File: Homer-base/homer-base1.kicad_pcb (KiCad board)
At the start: 2 copper layers, 16 parts

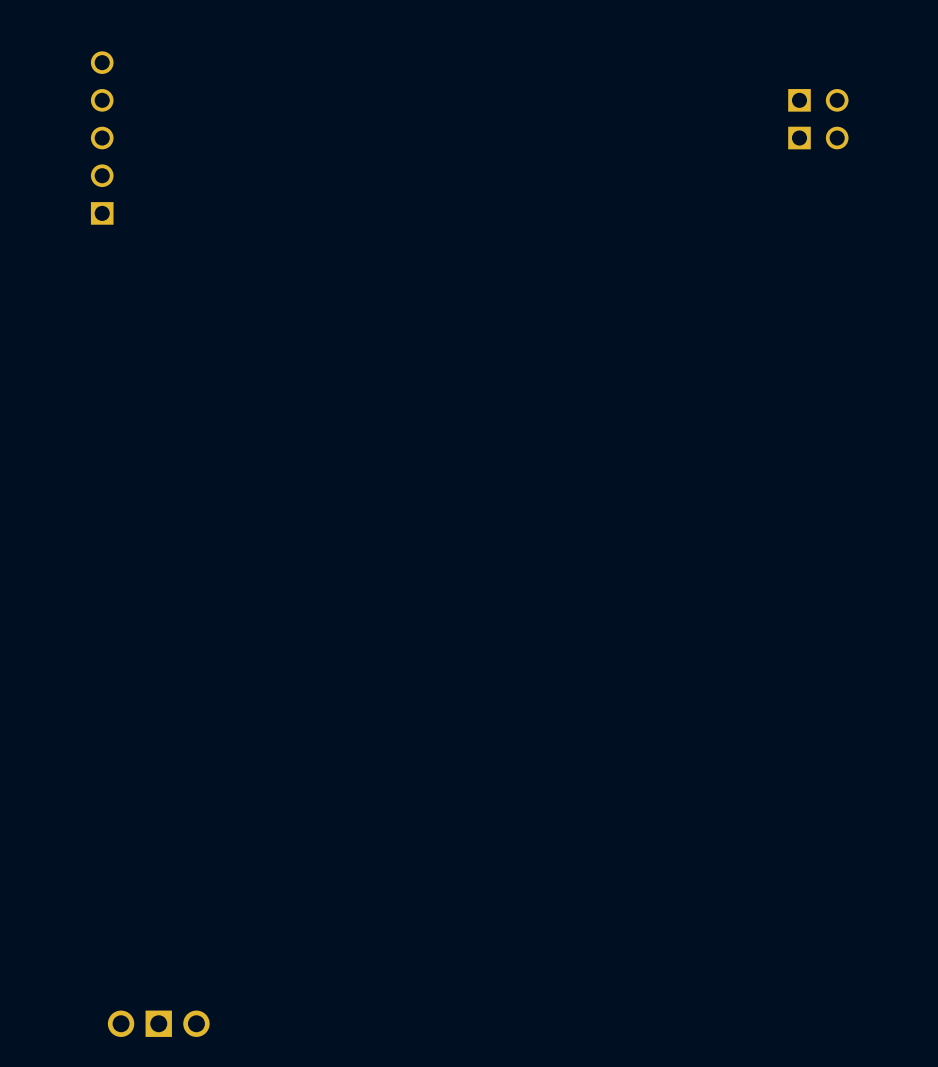
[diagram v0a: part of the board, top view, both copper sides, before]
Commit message: Add varistor and AC/DC
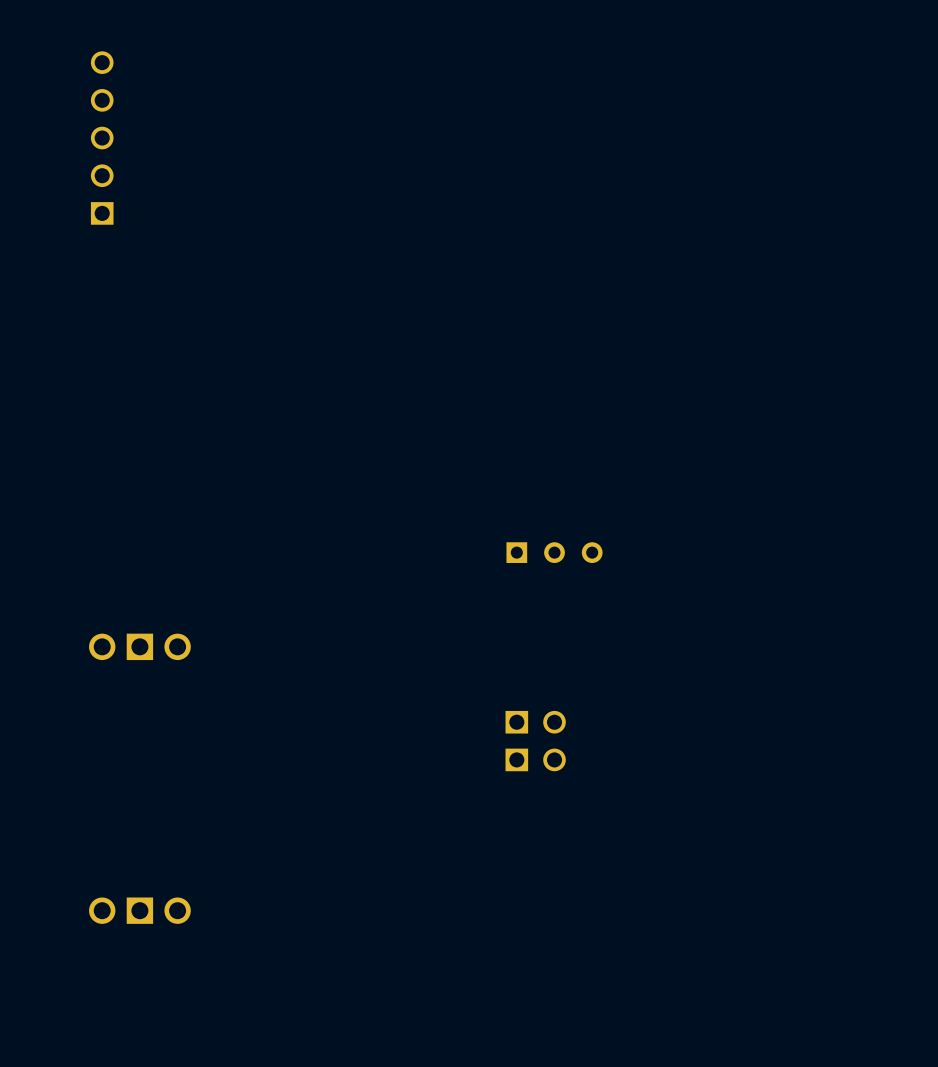
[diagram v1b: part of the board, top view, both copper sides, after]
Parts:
- added LD1086D: , LM78XXV, F.Cu at (1.27, -789.9)
- added Selettore Power: Val**, SIL-3, F.Cu at (29.2, -796.3)
- moved ? 46.0 mm to (27.9, -784.9)
- moved RS232 46.0 mm to (27.9, -782.3)
- moved LM7805V 7.73 mm to (1.27, -772.2)
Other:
- board text added: "220V"
- board text added: "3,6V,NC,NC,NC,B4,B2,SCA,RST"
- board text added: "6V"
- board text added: "GND,NC,NC,B5,B3,B1,SCL,BL"
- board text removed: "3,6V"
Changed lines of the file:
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@@
     (area -31.03245 -878.940001 169.316401 -756.819999)
     (thickness 1.6)
-    (drawings 27)
+    (drawings 29)
     (tracks 0)
     (zones 0)
-    (modules 16)
+    (modules 18)
     (nets 23)
   )
@@
     (add_net VCC)
   )
+  (module LM78XXV (layer "Rame Fronte")
+    (at 1.27 -789.94 270)
+    (descr "Regulateur TO220 serie LM78xx")
+    (tags "TR TO220")
+    (fp_text reference LD1086D (at 3.81 0 360) (layer "Serigrafia Fronte")
+      (effects (font (size 1.524 1.016) (thickness 0.2032)))
+    )
+    (fp_text value "" (at -3.175 -0.635 360) (layer "Serigrafia Fronte")
+      (effects (font (size 1.524 1.016) (thickness 0.2032)))
+    )
+    (fp_line (start 1.905 -4.445) (end 2.54 -4.445) (layer "Serigrafia Fronte") (width 0.254))
+    (fp_line (start 2.54 -4.445) (end 2.54 4.445) (layer "Serigrafia Fronte") (width 0.254))
+    (fp_line (start 2.54 4.445) (end 1.905 4.445) (layer "Serigrafia Fronte") (width 0.254))
+    (fp_line (start -1.905 -4.445) (end 1.905 -4.445) (layer "Serigrafia Fronte") (width 0.254))
+    (fp_line (start 1.905 -4.445) (end 1.905 4.445) (layer "Serigrafia Fronte") (width 0.254))
+    (fp_line (start 1.905 4.445) (end -1.905 4.445) (layer "Serigrafia Fronte") (width 0.254))
+    (fp_line (start -1.905 4.445) (end -1.905 -4.445) (layer "Serigrafia Fronte") (width 0.254))
+    (pad VI thru_hole circle (at 0 -2.54 270) (size 1.778 1.778) (drill 1.143)
+      (layers *.Cu *.Mask "Serigrafia Fronte")
+    )
+    (pad GND thru_hole rect (at 0 0 270) (size 1.778 1.778) (drill 1.143)
+      (layers *.Cu *.Mask "Serigrafia Fronte")
+    )
+    (pad VO thru_hole circle (at 0 2.54 270) (size 1.778 1.778) (drill 1.143)
+      (layers *.Cu *.Mask "Serigrafia Fronte")
+    )
+  )
   (module VASCH8x2 (layer "Rame Fronte")
     (at 6.35 -852.17 180)
@@
   )
   (module PIN_ARRAY_2X1 (layer "Rame Fronte")
-    (at 46.99 -826.77)
+    (at 27.94 -784.86)
     (descr "Connecteurs 2 pins")
     (tags "CONN DEV")
@@
   )
   (module PIN_ARRAY_2X1   placed (layer "Rame Fronte")
-    (at 46.99 -824.23)
+    (at 27.94 -782.32)
     (descr "Connecteurs 2 pins")
     (tags "CONN DEV")
@@
   )
   (module LM78XXV (layer "Rame Fronte")
-    (at 2.54 -764.54 270)
+    (at 1.27 -772.16 270)
     (descr "Regulateur TO220 serie LM78xx")
     (tags "TR TO220")
@@
     )
   )
+  (module SIL-3 (layer "Rame Fronte")
+    (at 29.21 -796.29)
+    (descr "Connecteur 3 pins")
+    (tags "CONN DEV")
+    (fp_text reference "Selettore Power" (at 0 -3.81) (layer "Serigrafia Fronte")
+      (effects (font (size 1.7907 1.07696) (thickness 0.26924)))
+    )
+    (fp_text value Val** (at 0 -2.54) (layer "Serigrafia Fronte") hide
+      (effects (font (size 1.524 1.016) (thickness 0.3048)))
+    )
+    (fp_line (start -3.81 1.27) (end -3.81 -1.27) (layer "Serigrafia Fronte") (width 0.3048))
+    (fp_line (start -3.81 -1.27) (end 3.81 -1.27) (layer "Serigrafia Fronte") (width 0.3048))
+    (fp_line (start 3.81 -1.27) (end 3.81 1.27) (layer "Serigrafia Fronte") (width 0.3048))
+    (fp_line (start 3.81 1.27) (end -3.81 1.27) (layer "Serigrafia Fronte") (width 0.3048))
+    (fp_line (start -1.27 -1.27) (end -1.27 1.27) (layer "Serigrafia Fronte") (width 0.3048))
+    (pad 1 thru_hole rect (at -2.54 0) (size 1.397 1.397) (drill 0.8128)
+      (layers *.Cu *.Mask "Serigrafia Fronte")
+    )
+    (pad 2 thru_hole circle (at 0 0) (size 1.397 1.397) (drill 0.8128)
+      (layers *.Cu *.Mask "Serigrafia Fronte")
+    )
+    (pad 3 thru_hole circle (at 2.54 0) (size 1.397 1.397) (drill 0.8128)
+      (layers *.Cu *.Mask "Serigrafia Fronte")
+    )
+  )
+  (gr_text 6V (at 21.59 -796.29) (layer "Serigrafia Fronte")
+    (effects (font (size 1.5 1.5) (thickness 0.3)))
+  )
+  (gr_text 220V (at 36.83 -796.29) (layer "Serigrafia Fronte")
+    (effects (font (size 1.5 1.5) (thickness 0.3)))
+  )
   (gr_text LV (at 83.82 -814.07) (layer "Serigrafia Fronte")
     (effects (font (size 1.5 1.5) (thickness 0.3)))
@@
     (effects (font (size 1.5 1.5) (thickness 0.3)))
   )
-  (gr_text "3,3V BLU/NERO" (at 10.16 -829.31) (layer "Serigrafia Fronte")
-    (effects (font (size 1.5 1.5) (thickness 0.3)))
-  )
-  (gr_text GND (at 3.81 -819.15) (layer "Serigrafia Fronte")
-    (effects (font (size 1.5 1.5) (thickness 0.3)))
-  )
-  (gr_text "3,6V GIALLO/BLU" (at 10.16 -826.77) (layer "Serigrafia Fronte")
-    (effects (font (size 1.5 1.5) (thickness 0.3)))
-  )
-  (gr_text 1 (at 16.51 -858.52) (layer "Serigrafia Fronte")
+  (gr_text "3,3V BLU/NERO" (at 10.16 -819.15) (layer "Serigrafia Fronte")
+    (effects (font (size 1.5 1.5) (thickness 0.3)))
+  )
+  (gr_text GND (at 3.81 -829.31) (layer "Serigrafia Fronte")
+    (effects (font (size 1.5 1.5) (thickness 0.3)))
+  )
+  (gr_text "3,6V GIALLO/BLU" (at 11.43 -821.69) (layer "Serigrafia Fronte")
+    (effects (font (size 1.5 1.5) (thickness 0.3)))
+  )
+  (gr_text 1 (at 21.59 -854.71) (layer "Serigrafia Fronte")
     (effects (font (size 1.5 1.5) (thickness 0.3)))
   )
@@
     (effects (font (size 1.5 1.5) (thickness 0.3)))
   )
-  (gr_text 3,6V (at -3.81 -845.82) (layer "Serigrafia Fronte")
-    (effects (font (size 1.5 1.5) (thickness 0.3)))
-  )
-  (gr_text GND (at -3.81 -858.52) (layer "Serigrafia Fronte")
-    (effects (font (size 1.5 1.5) (thickness 0.3)))
-  )
-  (gr_text "ACQUA-A5 TX" (at 58.42 -824.23) (layer "Serigrafia Fronte")
-    (effects (font (size 1.5 1.5) (thickness 0.3)))
-  )
-  (gr_text "ACQUA-A5 RX" (at 58.42 -826.77) (layer "Serigrafia Fronte")
-    (effects (font (size 1.5 1.5) (thickness 0.3)))
-  )
+  (gr_text 3,6V,NC,NC,NC,B4,B2,SCA,RST (at 6.35 -845.82) (layer "Serigrafia Fronte")
+    (effects (font (size 1.5 1.5) (thickness 0.3)))
+  )
+  (gr_text GND,NC,NC,B5,B3,B1,SCL,BL (at 6.35 -858.52) (layer "Serigrafia Fronte")
+    (effects (font (size 1.5 1.5) (thickness 0.3)))
+  )
+  (gr_text "ACQUA-A5 TX" (at 39.37 -782.32) (layer "Serigrafia Fronte")
+    (effects (font (size 1.5 1.5) (thickness 0.3)))
+  )
+  (gr_text "ACQUA-A5 RX" (at 39.37 -784.86) (layer "Serigrafia Fronte")
+    (effects (font (size 1.5 1.5) (thickness 0.3)))
+  )

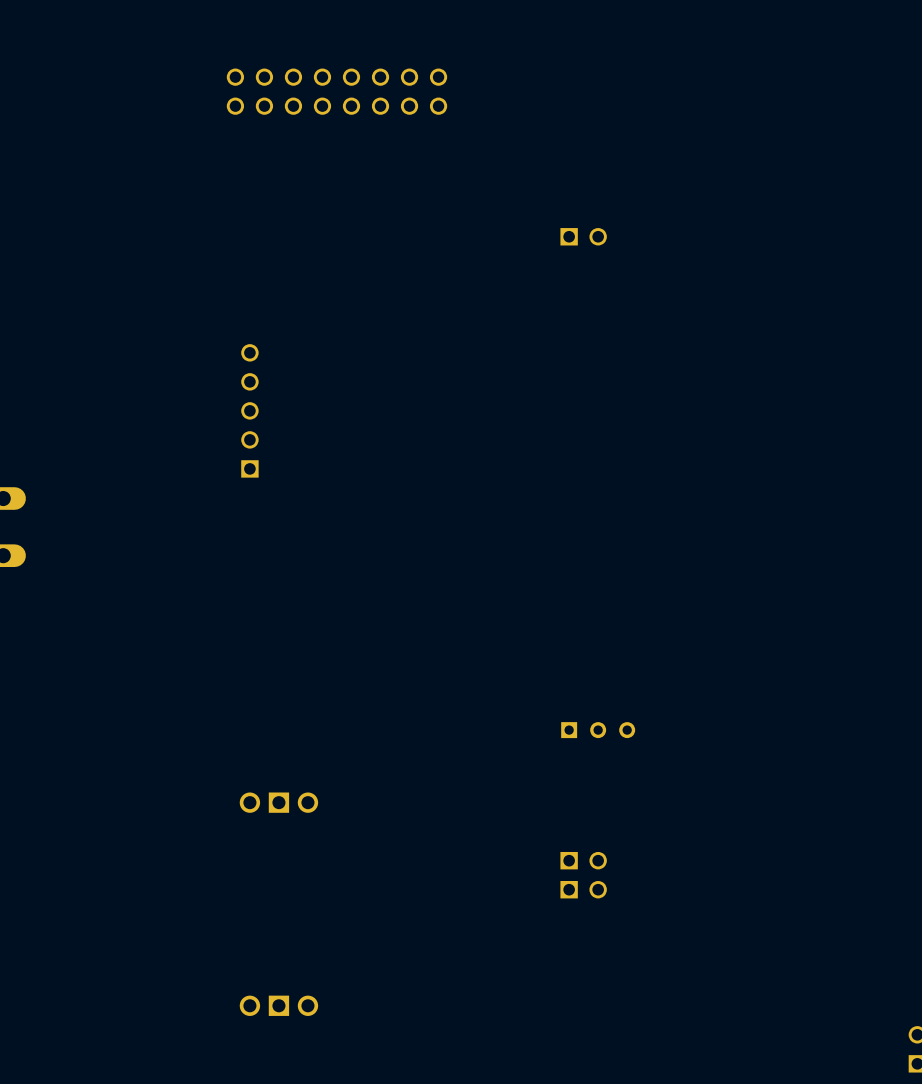
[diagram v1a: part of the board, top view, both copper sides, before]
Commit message: New power supply subsystem
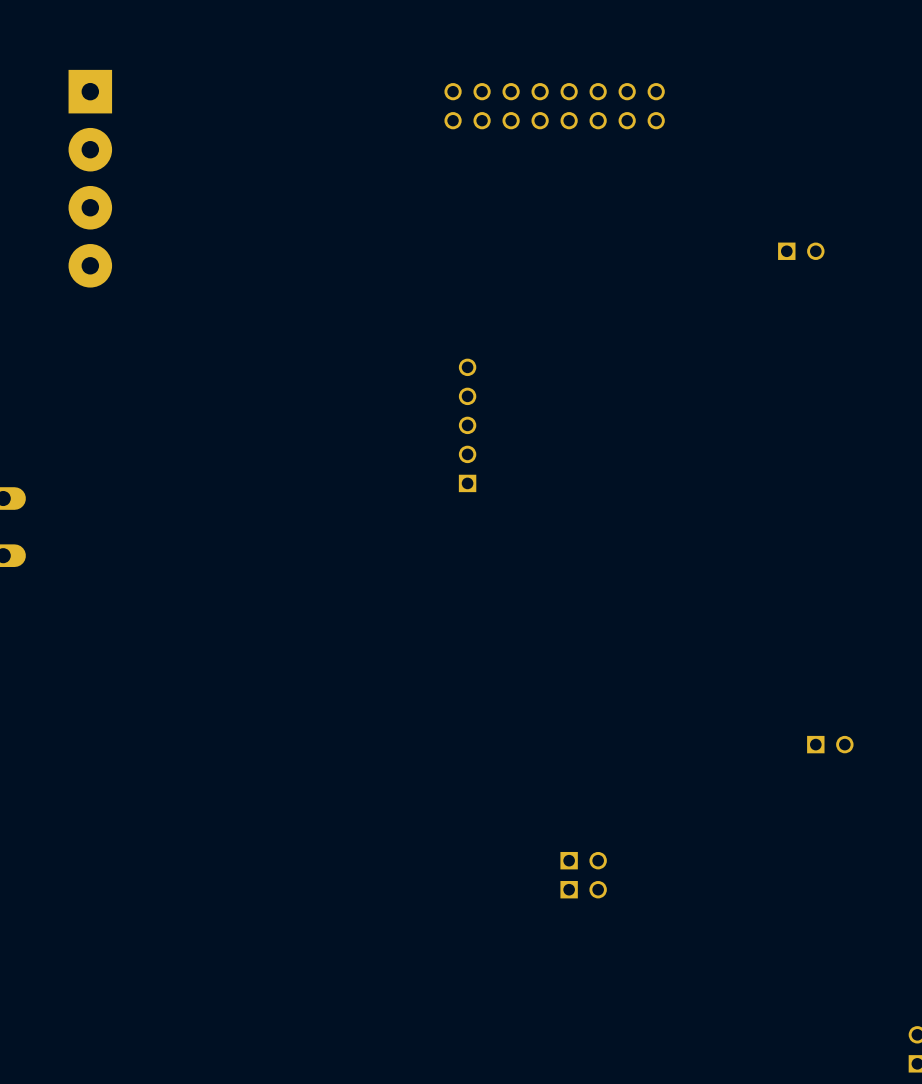
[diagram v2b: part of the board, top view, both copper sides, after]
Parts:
- removed LD1086D, LM7805V: , LM78XXV
- removed Selettore Power: Val**, SIL-3
- added P***: BORN4, bornier4, F.Cu at (-15.2, -844.5)
- added PIN_ARRAY_2: Val**, PIN_ARRAY_2X1, F.Cu at (49.5, -795.0)
- moved I2C TP 19.1 mm to (47.0, -838.2)
- moved POWER TPs 19.1 mm to (17.8, -823.0)
- moved ? 19.1 mm to (25.4, -850.9)
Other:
- board text added: "3,3V"
- board text added: "3,3V da Acqua-A5"
- board text added: "3,6V"
- board text added: "5V"
- board text removed: "220V"
- board text removed: "6V"

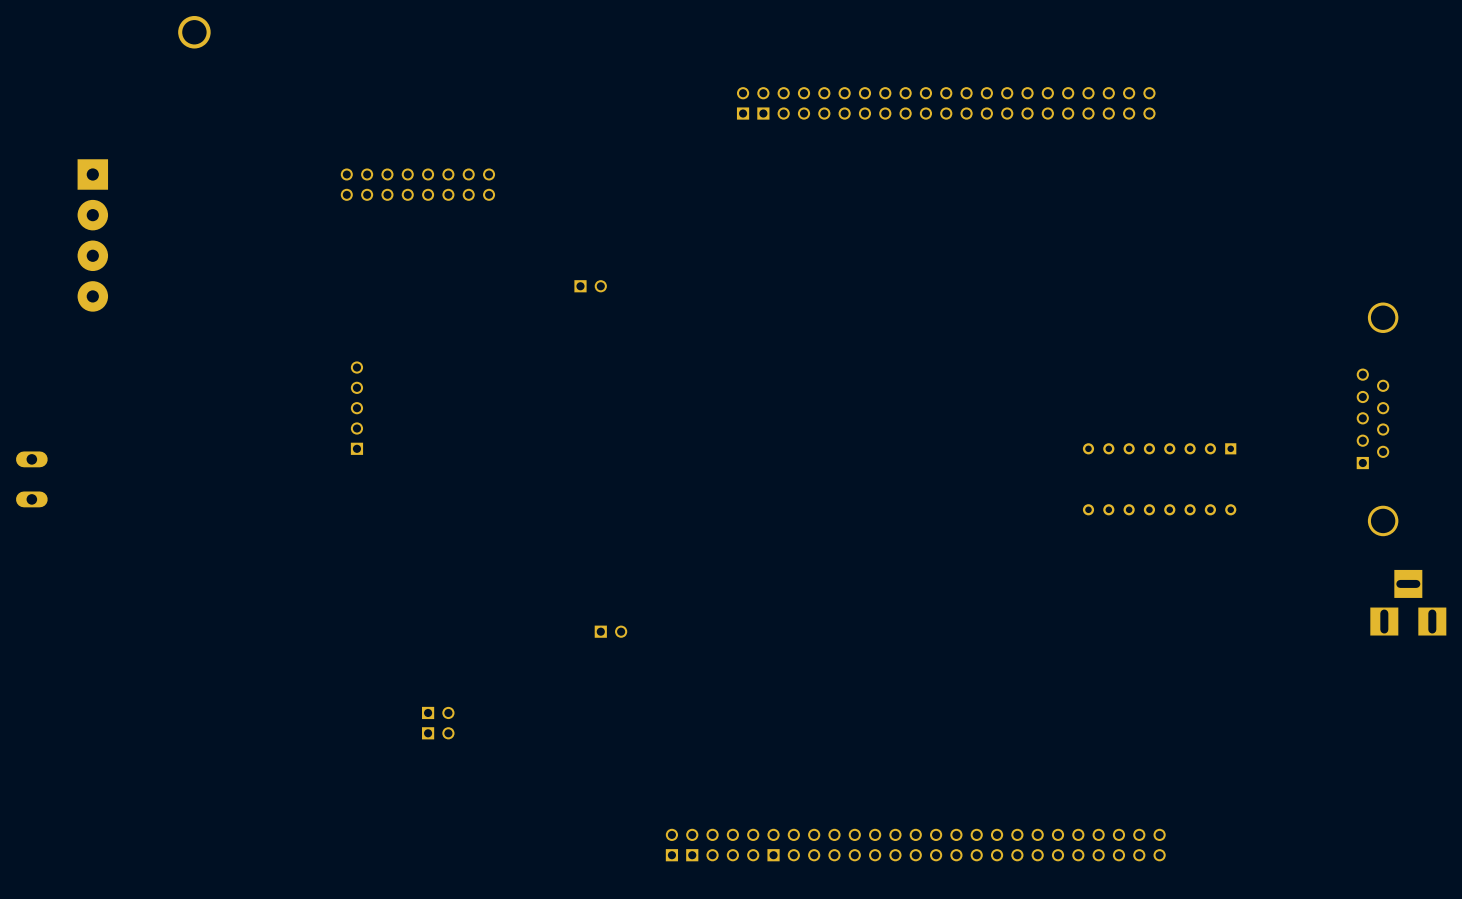
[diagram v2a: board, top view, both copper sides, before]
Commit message: Add current sensor, RTC battery, Power protection
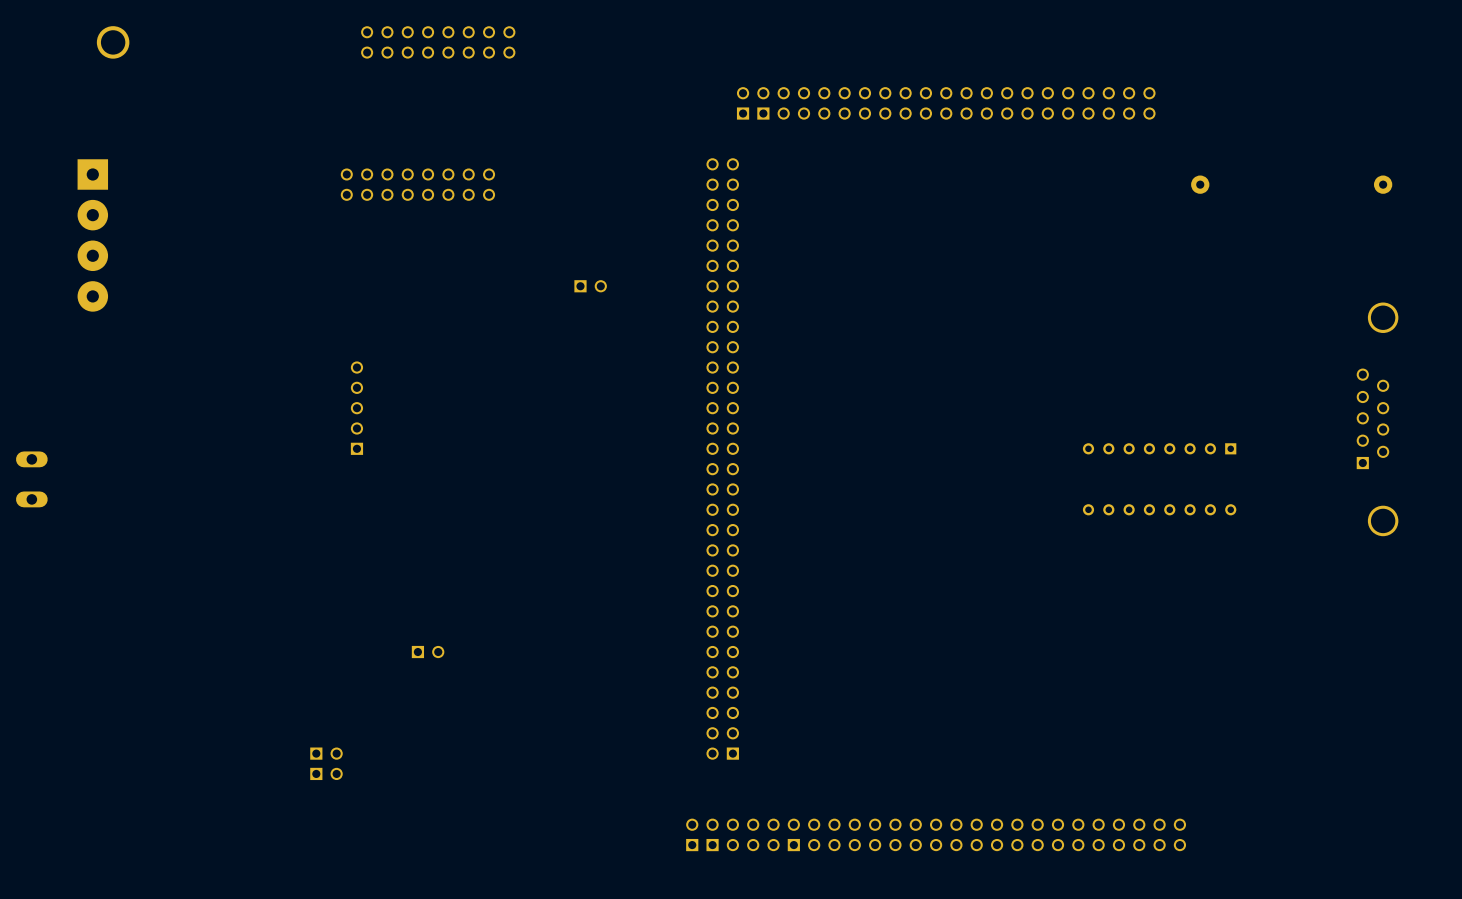
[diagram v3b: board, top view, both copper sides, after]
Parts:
- removed 6V IN: BARREL_JACK, BARREL_JACK
- added ?: POWER BOARD, VASCH8x2, F.Cu at (27.9, -868.7)
- added CR2032H: VAL**, CR2032H, F.Cu at (138.4, -850.9)
- added J2: , PIN_ARRAY_30X2, F.Cu at (63.5, -816.6)
- moved PIN_ARRAY_2 23.0 mm to (26.7, -792.5)
- moved ? 14.9 mm to (14.0, -779.8)
- moved RS232 14.9 mm to (14.0, -777.2)
- moved 1PIN 10.2 mm to (-12.7, -868.7)
- moved ? 2.84 mm to (66.0, -769.6)
- moved ? 2.84 mm to (59.7, -769.6)
- moved ? 2.84 mm to (96.5, -769.6)
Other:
- board text added: "NC,NC,NC,NC,NC,NC,NC,SCA"
- board text added: "NC,NC,NC,NC,NC,NC,NC,SCL"
